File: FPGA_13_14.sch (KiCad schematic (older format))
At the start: 15 parts, among them SW1 SW_DIP_x01, U1 XC7A200T-FBG484, U11 SN74LVC1G125DCKT, U30 S25FL128SAGMFIR01

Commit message: DDR terminations changed, HTML BoM with variant added
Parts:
- removed R209, R210: 0, Resistors SMD:RESC1005X40N, symbol AMC_FMC_Carrier-PcbDoc-rescue:R-Device
- added R209, R210: R0402_0R_JUMPER, RESC1005X40N, symbol Resistors_SMD:R0402_0R_JUMPER
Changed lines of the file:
@@
-EESchema Schematic File Version 5
+EESchema Schematic File Version 4
 LIBS:AMC_FMC_Carrier-PcbDoc-cache
 EELAYER 29 0
@@
 Comment4 ""
 $EndDescr
-BusAlias rgt rg g r
 $Comp
 L AMC_FMC_Carrier-PcbDoc-rescue:XC7A200T-FBG484-FPGA_Xilinx_Artix7 U?
@@
 Wire Wire Line
 	12000 1250 13200 1250
-$Comp
-L AMC_FMC_Carrier-PcbDoc-rescue:R-Device R?
-U 1 1 5C821907
-P 12500 1550
-AR Path="/5BD32060/5C821907" Ref="R?"  Part="1"
-AR Path="/5BABAC65/5C821907" Ref="R?"  Part="1"
-AR Path="/5CC24E97/5C821907" Ref="R?"  Part="1"
-AR Path="/5CC393D3/5C821907" Ref="R?"  Part="1"
-AR Path="/5CC6DBF7/5C821907" Ref="R?"  Part="1"
-AR Path="/5CC8AFE1/5C821907" Ref="R?"  Part="1"
-AR Path="/5BCEDA3D/5C821907" Ref="R?"  Part="1"
-AR Path="/5BCEDA39/5C821907" Ref="R?"  Part="1"
-AR Path="/5D05A99E/5C821907" Ref="R?"  Part="1"
-AR Path="/5C907554/5CC8CB69/5C821907" Ref="R209"  Part="1"
-F 0 "R209" V 12550 1850 50  0000 R CNN
-F 1 "0" V 12550 1400 50  0000 L CNN
-F 2 "Resistors SMD:RESC1005X40N" V 12430 1550 50  0001 C CNN
-F 3 "~" H 12500 1550 50  0001 C CNN
-F 4 "DNP" V 12550 1300 50  0000 C CNN "PN"
-	1    12500 1550
-	0    -1   -1   0
-$EndComp
-$Comp
-L AMC_FMC_Carrier-PcbDoc-rescue:R-Device R?
-U 1 1 5C831667
-P 12500 1650
-AR Path="/5BD32060/5C831667" Ref="R?"  Part="1"
-AR Path="/5BABAC65/5C831667" Ref="R?"  Part="1"
-AR Path="/5CC24E97/5C831667" Ref="R?"  Part="1"
-AR Path="/5CC393D3/5C831667" Ref="R?"  Part="1"
-AR Path="/5CC6DBF7/5C831667" Ref="R?"  Part="1"
-AR Path="/5CC8AFE1/5C831667" Ref="R?"  Part="1"
-AR Path="/5BCEDA3D/5C831667" Ref="R?"  Part="1"
-AR Path="/5BCEDA39/5C831667" Ref="R?"  Part="1"
-AR Path="/5D05A99E/5C831667" Ref="R?"  Part="1"
-AR Path="/5C907554/5CC8CB69/5C831667" Ref="R210"  Part="1"
-F 0 "R210" V 12550 1950 50  0000 R CNN
-F 1 "0" V 12550 1500 50  0000 L CNN
-F 2 "Resistors SMD:RESC1005X40N" V 12430 1650 50  0001 C CNN
-F 3 "~" H 12500 1650 50  0001 C CNN
-F 4 "DNP" V 12550 1400 50  0000 C CNN "PN"
-	1    12500 1650
-	0    -1   -1   0
-$EndComp
 Wire Wire Line
 	12650 1550 13200 1550
@@
 NoConn ~ 10500 8000
 NoConn ~ 6500 3100
+$Comp
+L Resistors_SMD:R0402_0R_JUMPER R?
+U 1 1 5CDA6911
+P 12350 1550
+AR Path="/5BCEDA39/5CDA6911" Ref="R?"  Part="1"
+AR Path="/5C907554/5CC8CB69/5CDA6911" Ref="R209"  Part="1"
+F 0 "R209" H 12300 1600 50  0000 C CNN
+F 1 "R0402_0R_JUMPER" H 12350 1340 60  0001 L CNN
+F 2 "RESC1005X40N" H 12350 530 60  0001 L CNN
+F 3 "\\\\cern.ch\\dfs\\Applications\\Altium\\Datasheets\\R0402_Phycomp_RC0402.pdf" H 12350 1160 60  0001 L CNN
+F 4 "0" H 12650 1600 50  0000 C CNN "~"
+F 5 "R0402_0R_JUMPER" H 12350 1070 60  0001 L CNN "Part Number"
+F 6 "Resistor" H 12350 980 60  0001 L CNN "Library Ref"
+F 7 "SchLib\\Resistors.SchLib" H 12350 890 60  0001 L CNN "Library Path"
+F 8 "=Value" H 12350 800 60  0001 L CNN "Comment"
+F 9 "Standard" H 12350 710 60  0001 L CNN "Component Kind"
+F 10 "Standard" H 12350 620 60  0001 L CNN "Component Type"
+F 11 "~~" H 12350 440 60  0001 L CNN "PackageDescription"
+F 12 "2" H 12350 350 60  0001 L CNN "Pin Count"
+F 13 "PcbLib\\Resistors SMD.PcbLib" H 12350 260 60  0001 L CNN "Footprint Path"
+F 14 "RESC1005X40N" H 12350 170 60  0001 L CNN "Footprint Ref"
+F 15 "0" H 12350 80  60  0001 L CNN "Val"
+F 16 "Not Recommended" H 12350 -10 60  0001 L CNN "Status"
+F 17 "~~" H 12350 -100 60  0001 L CNN "Power"
+F 18 "~~" H 12350 -190 60  0001 L CNN "TC"
+F 19 "~~" H 12350 -280 60  0001 L CNN "Voltage"
+F 20 "~~" H 12350 -370 60  0001 L CNN "Tolerance"
+F 21 "1A (0.05R Max DC Resistance) Zero Ohm Jumper" H 12350 -460 60  0001 L CNN "Part Description"
+F 22 "GENERIC" H 12350 -550 60  0001 L CNN "Manufacturer"
+F 23 "R0402_0R_JUMPER" H 12350 -640 60  0001 L CNN "Manufacturer Part Number"
+F 24 "0402" H 12350 -730 60  0001 L CNN "Case"
+F 25 "No" H 12350 -820 60  0001 L CNN "PressFit"
+F 26 "Yes" H 12350 -910 60  0001 L CNN "Mounted"
+F 27 "~~" H 12350 -1000 60  0001 L CNN "Sense Comment"
+F 28 "No" H 12350 -1090 60  0001 L CNN "Sense"
+F 29 "~~" H 12350 -1180 60  0001 L CNN "Status Comment"
+F 30 "No" H 12350 -1270 60  0001 L CNN "Socket"
+F 31 "Yes" H 12350 -1360 60  0001 L CNN "SMD"
+F 32 "~~" H 12350 -1450 60  0001 L CNN "ComponentHeight"
+F 33 "YAGEO PHYCOMP" H 12350 -1540 60  0001 L CNN "Manufacturer1 Example"
+F 34 "232270591001L" H 12350 -1630 60  0001 L CNN "Manufacturer1 Part Number"
+F 35 "0.4mm" H 12350 -1720 60  0001 L CNN "Manufacturer1 ComponentHeight"
+F 36 "\\\\cern.ch\\dfs\\Applications\\Altium\\Datasheets\\R0402_Phycomp_RC0402.pdf" H 12350 -1810 60  0001 L CNN "HelpURL"
+F 37 "CERN DEM JLC" H 12350 -1900 60  0001 L CNN "Author"
+F 38 "12/03/07 00:00:00" H 12350 -1990 60  0001 L CNN "CreateDate"
+F 39 "10/17/12 00:00:00" H 12350 -2080 60  0001 L CNN "LatestRevisionDate"
+F 40 "Resistors SMD" H 12350 -2170 60  0001 L CNN "Library Name"
+F 41 "This work is licensed under the Creative Commons CC-BY-SA 4.0 License. To the extent that circuit schematics that use Licensed Material can be considered to be ‘Adapted Material’, then the copyright holder waives article 3.b of the license with respect to these schematics." H 12350 -2260 60  0001 L CNN "License"
+F 42 "dnf" H 12750 1600 50  0000 C CNN "config"
+	1    12350 1550
+	1    0    0    -1
+$EndComp
+$Comp
+L Resistors_SMD:R0402_0R_JUMPER R?
+U 1 1 5CDA6B6E
+P 12350 1650
+AR Path="/5BCEDA39/5CDA6B6E" Ref="R?"  Part="1"
+AR Path="/5C907554/5CC8CB69/5CDA6B6E" Ref="R210"  Part="1"
+F 0 "R210" H 12300 1700 50  0000 C CNN
+F 1 "R0402_0R_JUMPER" H 12350 1440 60  0001 L CNN
+F 2 "RESC1005X40N" H 12350 630 60  0001 L CNN
+F 3 "\\\\cern.ch\\dfs\\Applications\\Altium\\Datasheets\\R0402_Phycomp_RC0402.pdf" H 12350 1260 60  0001 L CNN
+F 4 "0" H 12650 1700 50  0000 C CNN "~"
+F 5 "R0402_0R_JUMPER" H 12350 1170 60  0001 L CNN "Part Number"
+F 6 "Resistor" H 12350 1080 60  0001 L CNN "Library Ref"
+F 7 "SchLib\\Resistors.SchLib" H 12350 990 60  0001 L CNN "Library Path"
+F 8 "=Value" H 12350 900 60  0001 L CNN "Comment"
+F 9 "Standard" H 12350 810 60  0001 L CNN "Component Kind"
+F 10 "Standard" H 12350 720 60  0001 L CNN "Component Type"
+F 11 "~~" H 12350 540 60  0001 L CNN "PackageDescription"
+F 12 "2" H 12350 450 60  0001 L CNN "Pin Count"
+F 13 "PcbLib\\Resistors SMD.PcbLib" H 12350 360 60  0001 L CNN "Footprint Path"
+F 14 "RESC1005X40N" H 12350 270 60  0001 L CNN "Footprint Ref"
+F 15 "0" H 12350 180 60  0001 L CNN "Val"
+F 16 "Not Recommended" H 12350 90  60  0001 L CNN "Status"
+F 17 "~~" H 12350 0   60  0001 L CNN "Power"
+F 18 "~~" H 12350 -90 60  0001 L CNN "TC"
+F 19 "~~" H 12350 -180 60  0001 L CNN "Voltage"
+F 20 "~~" H 12350 -270 60  0001 L CNN "Tolerance"
+F 21 "1A (0.05R Max DC Resistance) Zero Ohm Jumper" H 12350 -360 60  0001 L CNN "Part Description"
+F 22 "GENERIC" H 12350 -450 60  0001 L CNN "Manufacturer"
+F 23 "R0402_0R_JUMPER" H 12350 -540 60  0001 L CNN "Manufacturer Part Number"
+F 24 "0402" H 12350 -630 60  0001 L CNN "Case"
+F 25 "No" H 12350 -720 60  0001 L CNN "PressFit"
+F 26 "Yes" H 12350 -810 60  0001 L CNN "Mounted"
+F 27 "~~" H 12350 -900 60  0001 L CNN "Sense Comment"
+F 28 "No" H 12350 -990 60  0001 L CNN "Sense"
+F 29 "~~" H 12350 -1080 60  0001 L CNN "Status Comment"
+F 30 "No" H 12350 -1170 60  0001 L CNN "Socket"
+F 31 "Yes" H 12350 -1260 60  0001 L CNN "SMD"
+F 32 "~~" H 12350 -1350 60  0001 L CNN "ComponentHeight"
+F 33 "YAGEO PHYCOMP" H 12350 -1440 60  0001 L CNN "Manufacturer1 Example"
+F 34 "232270591001L" H 12350 -1530 60  0001 L CNN "Manufacturer1 Part Number"
+F 35 "0.4mm" H 12350 -1620 60  0001 L CNN "Manufacturer1 ComponentHeight"
+F 36 "\\\\cern.ch\\dfs\\Applications\\Altium\\Datasheets\\R0402_Phycomp_RC0402.pdf" H 12350 -1710 60  0001 L CNN "HelpURL"
+F 37 "CERN DEM JLC" H 12350 -1800 60  0001 L CNN "Author"
+F 38 "12/03/07 00:00:00" H 12350 -1890 60  0001 L CNN "CreateDate"
+F 39 "10/17/12 00:00:00" H 12350 -1980 60  0001 L CNN "LatestRevisionDate"
+F 40 "Resistors SMD" H 12350 -2070 60  0001 L CNN "Library Name"
+F 41 "This work is licensed under the Creative Commons CC-BY-SA 4.0 License. To the extent that circuit schematics that use Licensed Material can be considered to be ‘Adapted Material’, then the copyright holder waives article 3.b of the license with respect to these schematics." H 12350 -2160 60  0001 L CNN "License"
+F 42 "dnf" H 12750 1700 50  0000 C CNN "config"
+	1    12350 1650
+	1    0    0    -1
+$EndComp
 $EndSCHEMATC

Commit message: SW2 placement changed, BOM cleared, FPGA boot, less ERC errors and wornings
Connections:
- wire segments 119 -> 122
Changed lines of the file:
@@
 L power:+2V5 #PWR?
 U 1 1 5C7D1417
-P 12000 900
+P 12000 850
 AR Path="/5C16BF8E/5C7D1417" Ref="#PWR?"  Part="1"
 AR Path="/5C907554/5C417BCB/5C7D1417" Ref="#PWR?"  Part="1"
 AR Path="/5C907554/5C7D1417" Ref="#PWR?"  Part="1"
 AR Path="/5C907554/5CC8CB69/5C7D1417" Ref="#PWR055"  Part="1"
-F 0 "#PWR055" H 12000 750 50  0001 C CNN
-F 1 "+2V5" H 12015 1073 50  0000 C CNN
-F 2 "" H 12000 900 50  0001 C CNN
-F 3 "" H 12000 900 50  0001 C CNN
-	1    12000 900
+F 0 "#PWR055" H 12000 700 50  0001 C CNN
+F 1 "+2V5" H 12015 1023 50  0000 C CNN
+F 2 "" H 12000 850 50  0001 C CNN
+F 3 "" H 12000 850 50  0001 C CNN
+	1    12000 850
 	1    0    0    -1
 $EndComp
@@
 Connection ~ 12750 1850
 Wire Wire Line
-	12750 1850 13200 1850
+	12750 1850 13100 1850
 $Comp
 L Capacitors_SMD:CC0201_100NF_6.3V_10%_X5R C?
@@
 	1    0    0    -1
 $EndComp
+$Comp
+L power:PWR_FLAG #FLG?
+U 1 1 5D5BD226
+P 13100 1850
+AR Path="/5BABAC65/5D5BD226" Ref="#FLG?"  Part="1"
+AR Path="/5C907554/5CC8CB69/5D5BD226" Ref="#FLG0136"  Part="1"
+F 0 "#FLG0136" H 13100 1925 50  0001 C CNN
+F 1 "PWR_FLAG" H 13100 2000 50  0000 C CNN
+F 2 "" H 13100 1850 50  0001 C CNN
+F 3 "~" H 13100 1850 50  0001 C CNN
+	1    13100 1850
+	1    0    0    -1
+$EndComp
+Connection ~ 13100 1850
+Wire Wire Line
+	13100 1850 13200 1850
+$Comp
+L power:PWR_FLAG #FLG?
+U 1 1 5D5C4CA6
+P 12450 2200
+AR Path="/5BABAC65/5D5C4CA6" Ref="#FLG?"  Part="1"
+AR Path="/5C907554/5CC8CB69/5D5C4CA6" Ref="#FLG0137"  Part="1"
+F 0 "#FLG0137" H 12450 2275 50  0001 C CNN
+F 1 "PWR_FLAG" H 12450 2373 50  0000 C CNN
+F 2 "" H 12450 2200 50  0001 C CNN
+F 3 "~" H 12450 2200 50  0001 C CNN
+	1    12450 2200
+	-1   0    0    1
+$EndComp
+Wire Wire Line
+	12450 2200 12450 2150
+Connection ~ 12450 2150
+Wire Wire Line
+	12000 850  12000 900
 $EndSCHEMATC

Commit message: BOM updated, 25MHz clock level fixed
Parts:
- SW1: symbol AMC_FMC_Carrier-PcbDoc-rescue:SW_DIP_x01-Switch -> AMC_FMC_Carrier-PcbDoc-rescue:SW_DIP_x01-Switch-AMC_FMC_Carrier-PcbDoc-rescue
- U1: symbol AMC_FMC_Carrier-PcbDoc-rescue:XC7A200T-FBG484-FPGA_Xilinx_Artix7 -> AMC_FMC_Carrier-PcbDoc-rescue:XC7A200T-FBG484-FPGA_Xilinx_Artix7-AMC_FMC_Carrier-PcbDoc-rescue
- U11: symbol AMC_FMC_Carrier-PcbDoc-rescue:SN74LVC1G125DCKT-Standard_Logic -> AMC_FMC_Carrier-PcbDoc-rescue:SN74LVC1G125DCKT-Standard_Logic-AMC_FMC_Carrier-PcbDoc-rescue
- U30: symbol AMC_FMC_Carrier-PcbDoc-rescue:S25FL128SAGMFIR01-powerMG -> AMC_FMC_Carrier-PcbDoc-rescue:S25FL128SAGMFIR01-powerMG-AMC_FMC_Carrier-PcbDoc-rescue
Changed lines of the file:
@@
 $EndDescr
 $Comp
-L AMC_FMC_Carrier-PcbDoc-rescue:XC7A200T-FBG484-FPGA_Xilinx_Artix7 U?
+L AMC_FMC_Carrier-PcbDoc-rescue:XC7A200T-FBG484-FPGA_Xilinx_Artix7-AMC_FMC_Carrier-PcbDoc-rescue U?
 U 1 1 5CC902F4
 P 8500 5200
@@
 	7200 2300 7100 2300
 $Comp
-L AMC_FMC_Carrier-PcbDoc-rescue:S25FL128SAGMFIR01-powerMG U30
+L AMC_FMC_Carrier-PcbDoc-rescue:S25FL128SAGMFIR01-powerMG-AMC_FMC_Carrier-PcbDoc-rescue U30
 U 1 1 5C40DA57
 P 13400 850
@@
 $EndComp
 $Comp
-L AMC_FMC_Carrier-PcbDoc-rescue:S25FL128SAGMFIR01-powerMG U30
+L AMC_FMC_Carrier-PcbDoc-rescue:S25FL128SAGMFIR01-powerMG-AMC_FMC_Carrier-PcbDoc-rescue U30
 U 2 1 5C40DA9C
 P 14700 850
@@
 	12650 1650 13200 1650
 $Comp
-L AMC_FMC_Carrier-PcbDoc-rescue:SW_DIP_x01-Switch SW1
+L AMC_FMC_Carrier-PcbDoc-rescue:SW_DIP_x01-Switch-AMC_FMC_Carrier-PcbDoc-rescue SW1
 U 1 1 5C881CE2
 P 13000 3200
@@
 $EndComp
 $Comp
-L AMC_FMC_Carrier-PcbDoc-rescue:SN74LVC1G125DCKT-Standard_Logic U11
+L AMC_FMC_Carrier-PcbDoc-rescue:SN74LVC1G125DCKT-Standard_Logic-AMC_FMC_Carrier-PcbDoc-rescue U11
 U 1 1 5C4235B4
 P 13850 3000

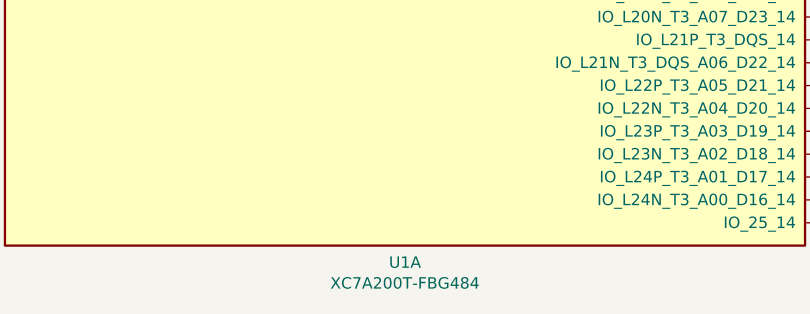
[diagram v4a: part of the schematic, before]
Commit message: BOM configuration file edited, updated Marble picture, some components part number changed
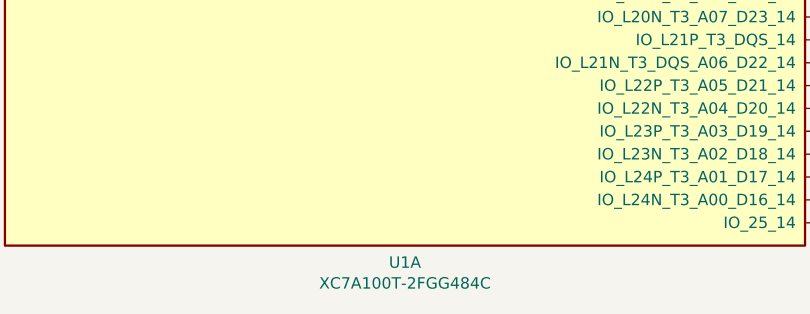
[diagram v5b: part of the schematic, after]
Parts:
- SW1: Manufacturer Part Number (none) -> A6SN-1101; PN OMRON_A6SN-1101 -> (none)
- U1: value XC7A200T-FBG484 -> XC7A100T-2FGG484C; Manufacturer Part Number (none) -> XC7A100T-2FGG484C
- U30: Manufacturer Part Number (none) -> S25FL128SAGMFIR01; PN S25FL128SAGMFIR01 -> (none)
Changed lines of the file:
@@
 $Descr A3 16535 11693
 encoding utf-8
-Sheet 22 25
+Sheet 21 25
 Title "Marble"
 Date "2019-01-16"
@@
 AR Path="/5C907554/5CC8CB69/5CC902F4" Ref="U1"  Part="1"
 F 0 "U1" H 8500 2226 50  0000 C CNN
-F 1 "XC7A200T-FBG484" H 8500 2135 50  0000 C CNN
+F 1 "XC7A100T-2FGG484C" H 8500 2135 50  0000 C CNN
 F 2 "ICs And Semiconductors SMD_BGA:BGA484C100P22X22_2300X2300X240" H 8500 5200 50  0001 C CNN
 F 3 "" H 8500 5200 50  0000 C CNN
+F 4 "XC7A100T-2FGG484C" H 8500 5200 50  0001 C CNN "Manufacturer Part Number"
 	1    8500 5200
 	1    0    0    -1
@@
 F 2 "ICs And Semiconductors SMD:SOIC127P1030X265-16N" H 13400 850 50  0001 C CNN
 F 3 "" H 13400 850 50  0001 C CNN
-F 4 "S25FL128SAGMFIR01" H 13400 850 50  0001 C CNN "PN"
+F 4 "S25FL128SAGMFIR01" H 13400 850 50  0001 C CNN "Manufacturer Part Number"
 	1    13400 850
 	1    0    0    -1
@@
 F 2 "ICs And Semiconductors SMD:SOIC127P1030X265-16N" H 14700 850 50  0001 C CNN
 F 3 "" H 14700 850 50  0001 C CNN
-F 4 "S25FL128SAGMFIR01" H 14700 850 50  0001 C CNN "PN"
+F 4 "S25FL128SAGMFIR01" H 14700 850 50  0001 C CNN "Manufacturer Part Number"
 	2    14700 850
 	1    0    0    -1
@@
 F 2 "Switches:SW_OMRON_A6SN-1101" H 13000 3200 50  0001 C CNN
 F 3 "" H 13000 3200 50  0001 C CNN
-F 4 "OMRON_A6SN-1101" H 13000 3200 50  0001 C CNN "PN"
+F 4 "A6SN-1101" H 13000 3200 50  0001 C CNN "Manufacturer Part Number"
 	1    13000 3200
 	-1   0    0    -1

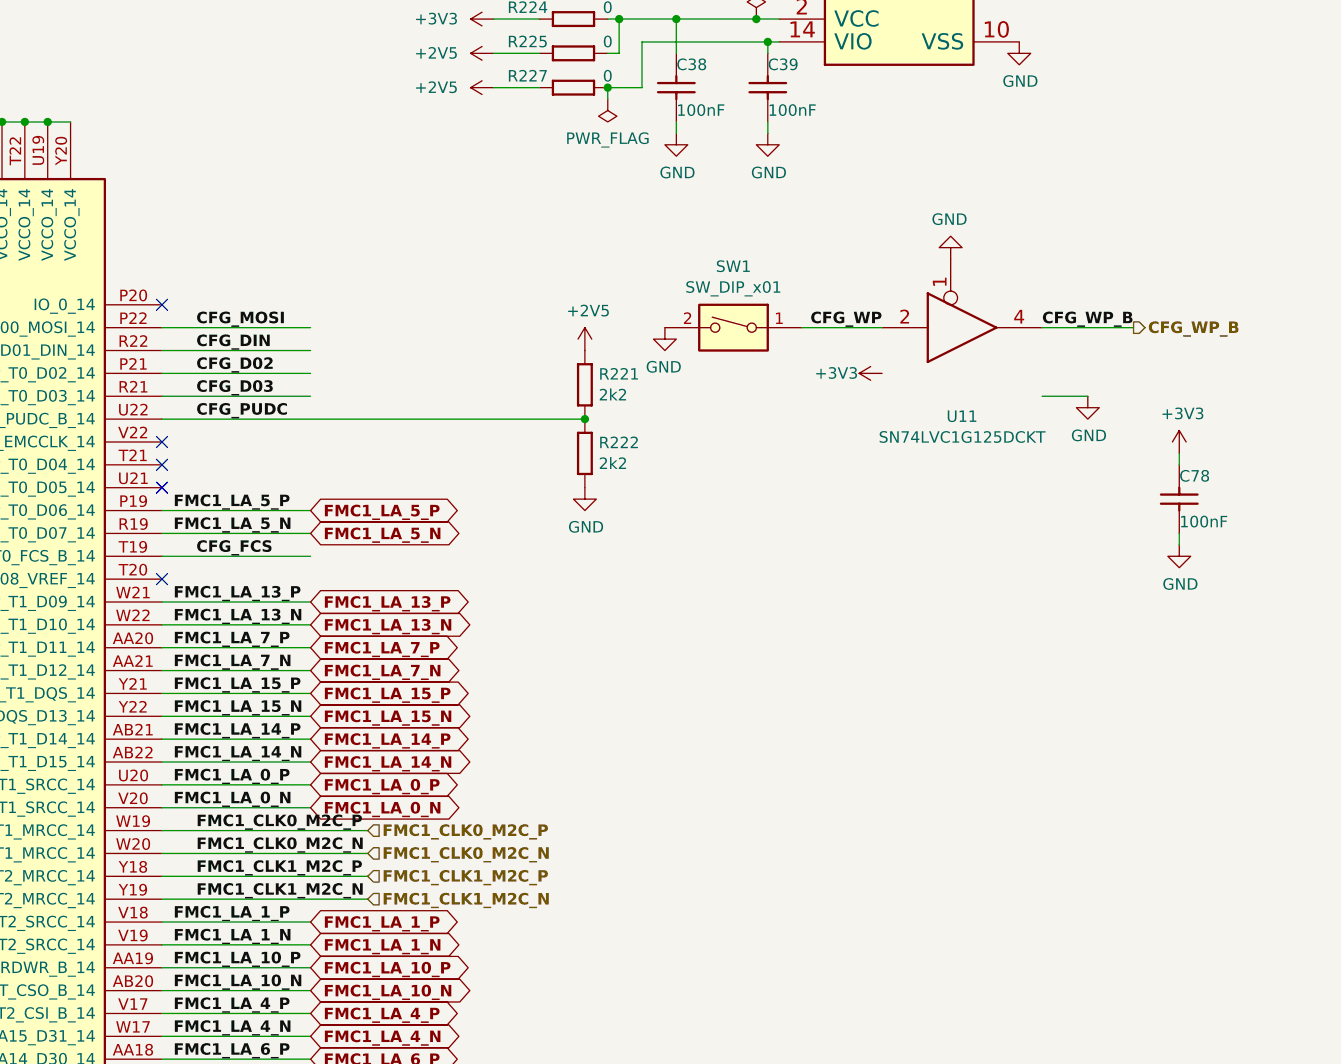
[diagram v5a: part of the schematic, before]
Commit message: R221->DNP, netlist_to_xdc.py updated
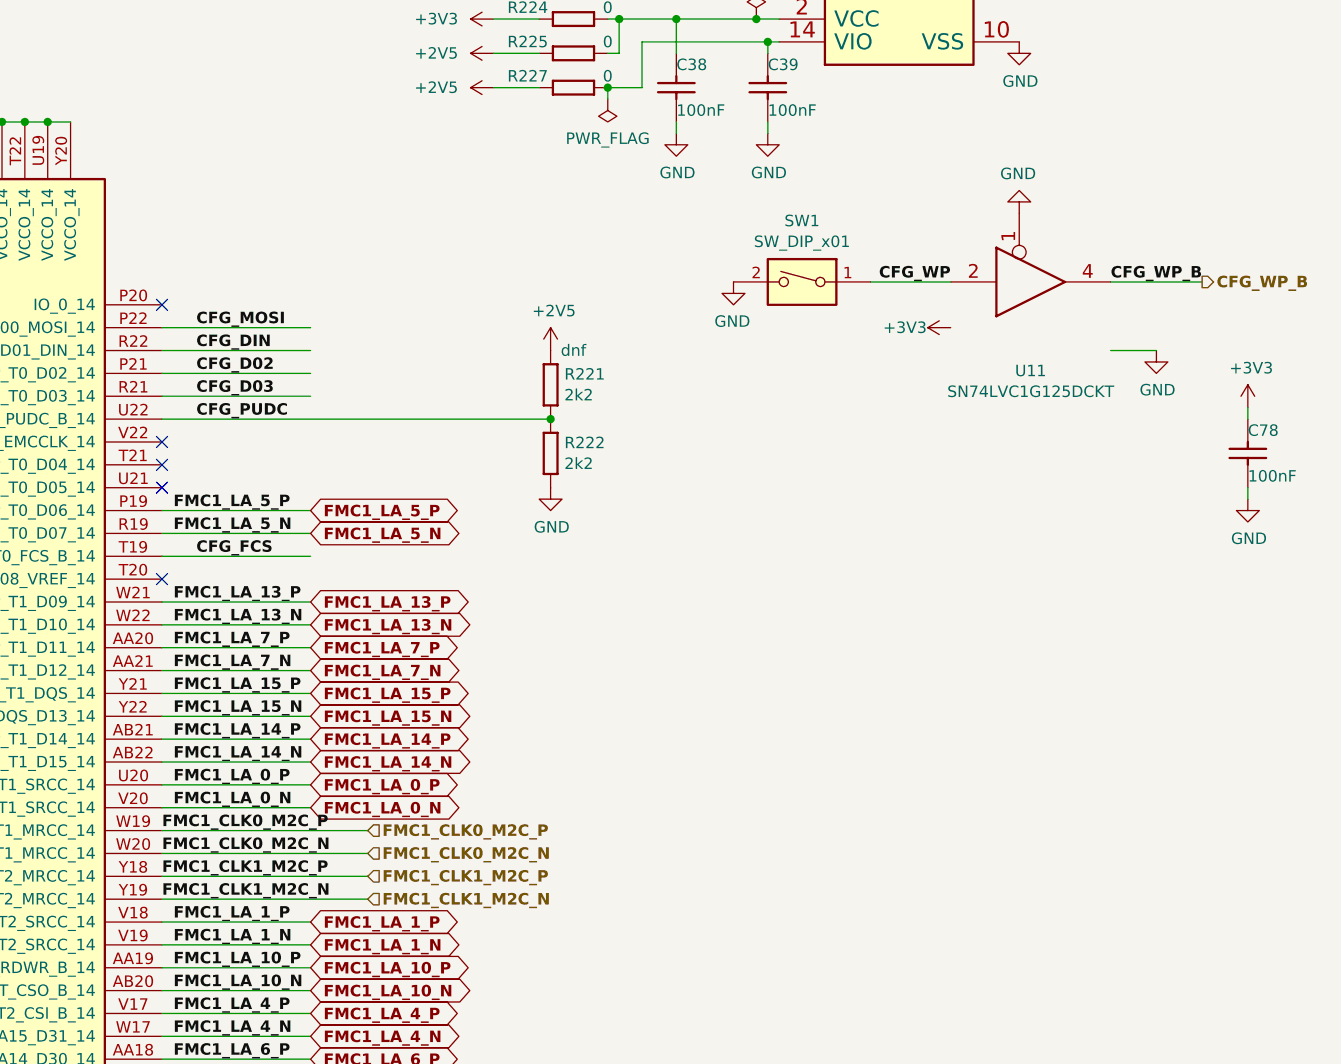
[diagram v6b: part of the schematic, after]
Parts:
- R221: config (none) -> dnf
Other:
- moved on the sheet: C78, R221, R222, SW1, U11

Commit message: applied all required amendments to the project
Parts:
- R225: config (none) -> dnf
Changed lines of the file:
@@
 EESchema Schematic File Version 4
 LIBS:AMC_FMC_Carrier-PcbDoc-cache
-EELAYER 29 0
+EELAYER 30 0
 EELAYER END
 $Descr A3 16535 11693
@@
 AR Path="/5C907554/5CAAC367/5F9465E2" Ref="R?"  Part="1"
 AR Path="/5C907554/5CC8CB69/5F9465E2" Ref="R221"  Part="1"
-F 0 "R221" V 12304 3360 50  0000 L CNN
+F 0 "R221" V 12300 3350 50  0000 L CNN
 F 1 "R0402_2K2_1%_0.0625W_100PPM" H 12200 3090 60  0001 L CNN
 F 2 "RESC1005X40N" H 12200 2280 60  0001 L CNN
@@
 F 40 "Resistors SMD" H 12200 -420 60  0001 L CNN "Library Name"
 F 41 "This work is licensed under the Creative Commons CC-BY-SA 4.0 License. To the extent that circuit schematics that use Licensed Material can be considered to be ‘Adapted Material’, then the copyright holder waives article 3.b of the license with respect to these schematics." H 12200 -510 60  0001 L CNN "License"
-F 42 "dnf" V 12200 3400 50  0000 C CNN "config"
+F 42 "dnf" V 12200 3350 50  0000 L CNN "config"
 	1    12200 3300
 	0    1    1    0
@@
 F 40 "Resistors SMD" H 12150 -1720 60  0001 L CNN "Library Name"
 F 41 "This work is licensed under the Creative Commons CC-BY-SA 4.0 License. To the extent that circuit schematics that use Licensed Material can be considered to be ‘Adapted Material’, then the copyright holder waives article 3.b of the license with respect to these schematics." H 12150 -1810 60  0001 L CNN "License"
+F 42 "dnf" H 12500 2000 50  0000 C CNN "config"
 	1    12150 2000
 	1    0    0    -1
